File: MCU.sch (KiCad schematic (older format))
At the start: 32 parts, among them J1 RX, J15 RESET, J16 ISP, J17 WS2812, J18 SJ-43514-SMT, J2 TX, J7 TYPE-C-31-M-12, SW1 EC11E, SW3 Reset, U1 ATmega32U4-AU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

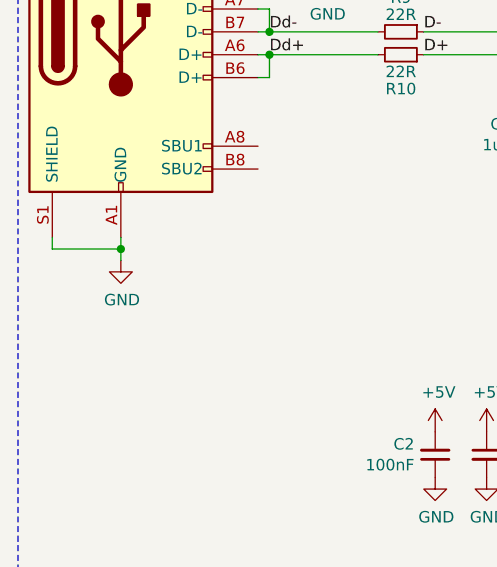
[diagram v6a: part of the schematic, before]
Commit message: Connected USB shield via RC filter, updated renders
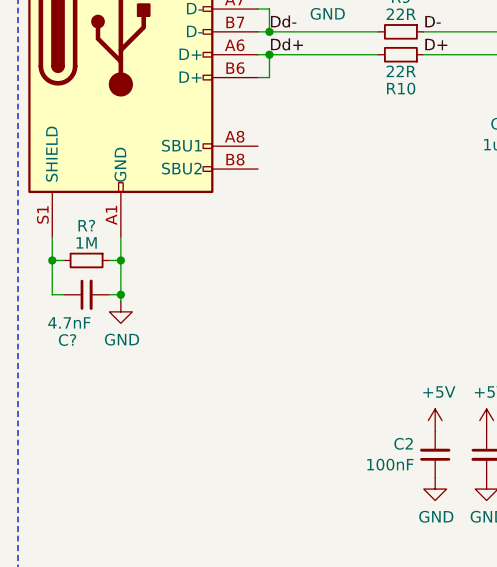
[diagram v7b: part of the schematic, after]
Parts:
- added C?: 4.7nF, Capacitor_SMD:C_0603_1608Metric_Pad1.05x0.95mm_HandSolder, symbol Device:C_Small
- added R?: 1M, Resistor_SMD:R_0603_1608Metric_Pad1.05x0.95mm_HandSolder, symbol Device:R_Small
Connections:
- net GND: now also C?.2, R?.1; no longer J7.S1 (SHIELD)
- new net: C?.1, J7.S1 (SHIELD), R?.2
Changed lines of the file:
@@
 L power:GND #PWR0105
 U 1 1 5DCBF496
-P 1700 3150
+P 1700 3325
 AR Path="/5DCB7F8C/5DCBF496" Ref="#PWR0105"  Part="1"
 AR Path="/5E0F7128/5DCBF496" Ref="#PWR0131"  Part="1"
-F 0 "#PWR0105" H 1700 2900 50  0001 C CNN
-F 1 "GND" H 1705 2977 50  0000 C CNN
-F 2 "" H 1700 3150 50  0001 C CNN
-F 3 "" H 1700 3150 50  0001 C CNN
-	1    1700 3150
-	1    0    0    -1
-$EndComp
-Wire Wire Line
-	1700 3050 1700 3100
-Wire Wire Line
-	1700 3100 1400 3100
-Wire Wire Line
-	1400 3100 1400 3050
-Connection ~ 1700 3100
-Wire Wire Line
-	1700 3100 1700 3150
+F 0 "#PWR0105" H 1700 3075 50  0001 C CNN
+F 1 "GND" H 1705 3152 50  0000 C CNN
+F 2 "" H 1700 3325 50  0001 C CNN
+F 3 "" H 1700 3325 50  0001 C CNN
+	1    1700 3325
+	1    0    0    -1
+$EndComp
 $Comp
 L Device:R_Small R9
@@
 Text Notes 2400 1525 0    50   ~ 0
 1A hold
+$Comp
+L Device:C_Small C?
+U 1 1 5DC857C3
+P 1550 3300
+AR Path="/5DCB7F8C/5DC857C3" Ref="C?"  Part="1"
+AR Path="/5E0F7128/5DC857C3" Ref="C?"  Part="1"
+F 0 "C?" V 1350 3425 50  0000 R CNN
+F 1 "4.7nF" V 1425 3375 50  0000 C CNN
+F 2 "Capacitor_SMD:C_0603_1608Metric_Pad1.05x0.95mm_HandSolder" H 1550 3300 50  0001 C CNN
+F 3 "~" H 1550 3300 50  0001 C CNN
+	1    1550 3300
+	0    -1   -1   0
+$EndComp
+Wire Wire Line
+	1700 3050 1700 3150
+$Comp
+L Device:R_Small R?
+U 1 1 5DCA8592
+P 1550 3150
+AR Path="/5DCB7F8C/5DCA8592" Ref="R?"  Part="1"
+AR Path="/5E0F7128/5DCA8592" Ref="R?"  Part="1"
+F 0 "R?" V 1400 3150 50  0000 C CNN
+F 1 "1M" V 1475 3150 50  0000 C CNN
+F 2 "Resistor_SMD:R_0603_1608Metric_Pad1.05x0.95mm_HandSolder" H 1550 3150 50  0001 C CNN
+F 3 "~" H 1550 3150 50  0001 C CNN
+	1    1550 3150
+	0    1    1    0
+$EndComp
+Wire Wire Line
+	1400 3150 1450 3150
+Wire Wire Line
+	1400 3050 1400 3150
+Wire Wire Line
+	1650 3150 1700 3150
+Wire Wire Line
+	1400 3150 1400 3300
+Wire Wire Line
+	1400 3300 1450 3300
+Connection ~ 1400 3150
+Wire Wire Line
+	1650 3300 1700 3300
+Wire Wire Line
+	1700 3300 1700 3150
+Connection ~ 1700 3150
+Wire Wire Line
+	1700 3325 1700 3300
+Connection ~ 1700 3300
 $EndSCHEMATC

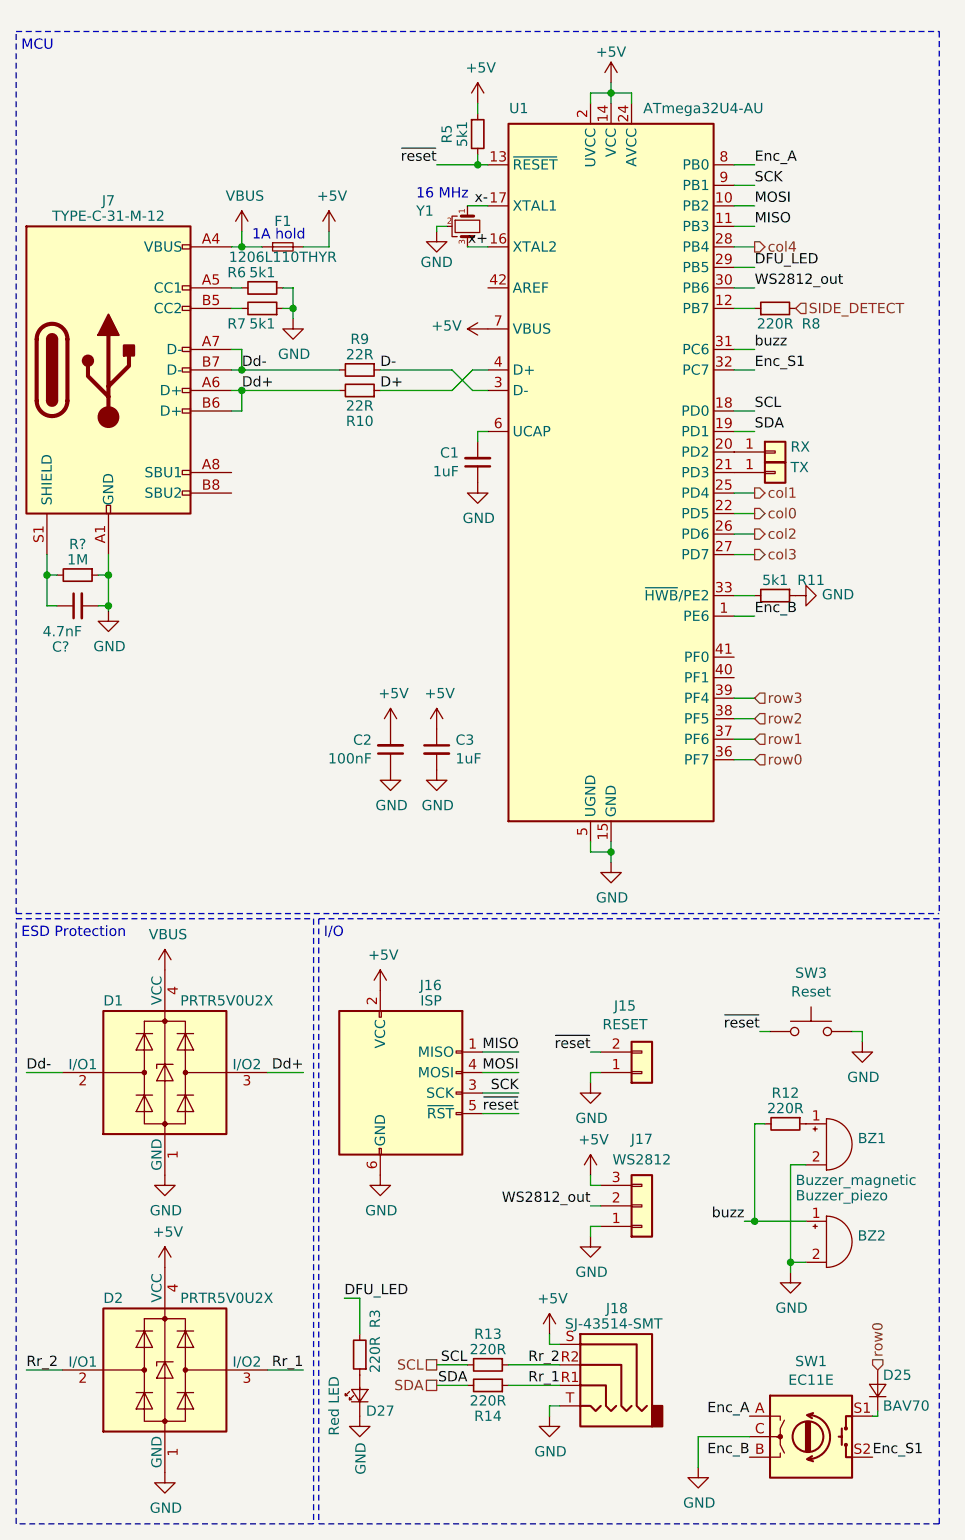
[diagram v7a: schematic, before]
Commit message: Swapped SDA and SCL pins on TRRS jack
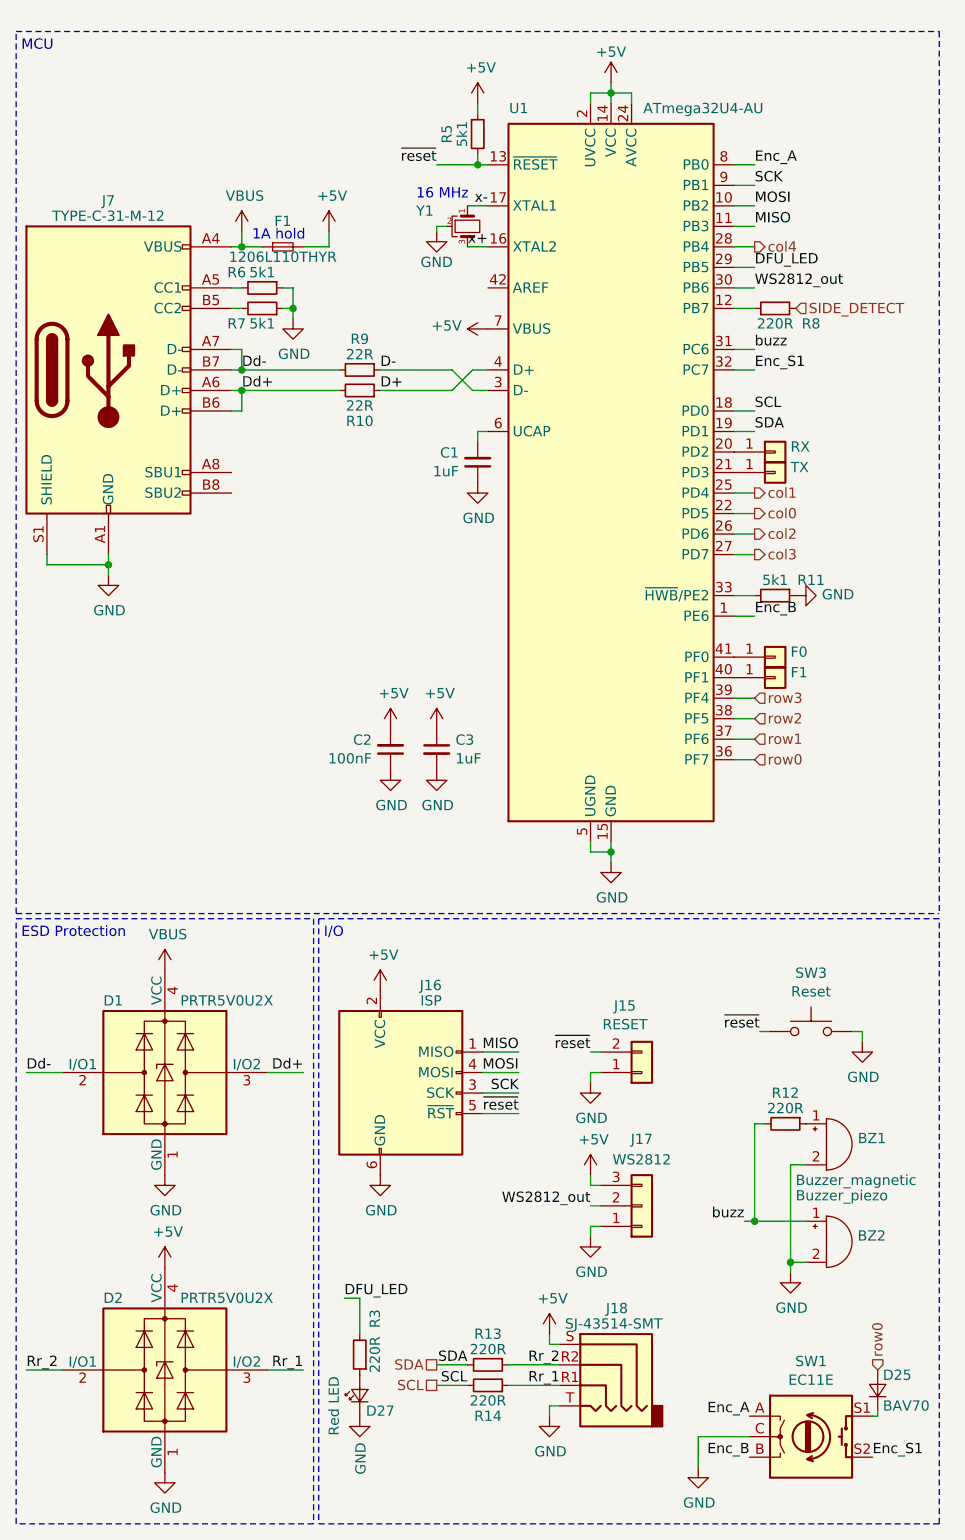
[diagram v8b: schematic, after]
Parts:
- removed C?: 4.7nF, Capacitor_SMD:C_0603_1608Metric_Pad1.05x0.95mm_HandSolder, symbol Device:C_Small
- removed R?: 1M, Resistor_SMD:R_0603_1608Metric_Pad1.05x0.95mm_HandSolder, symbol Device:R_Small
- added J?: F0, TestPoint:TestPoint_Pad_D1.0mm, symbol Connector_Generic:Conn_01x01
- added J?: F1, TestPoint:TestPoint_Pad_D1.0mm, symbol Connector_Generic:Conn_01x01
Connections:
- net GND: now also J7.S1 (SHIELD)
- net SCL: now also R14.2; no longer R13.2
- net SDA: now also R13.2; no longer R14.2
- net at U1.40 (PF1): now also J?.1 (Pin_1)
- net at U1.41 (PF0): now also J?.1 (Pin_1)
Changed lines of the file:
@@
 $EndDescr
-$Comp
-L Connector:USB_C_Receptacle_USB2.0 J7
-U 1 1 5DCB829A
-P 1700 2150
-AR Path="/5DCB7F8C/5DCB829A" Ref="J7"  Part="1"
-AR Path="/5E0F7128/5DCB829A" Ref="J25"  Part="1"
-F 0 "J7" H 1700 2975 50  0000 C CNN
-F 1 "TYPE-C-31-M-12" H 1700 2900 50  0000 C CNN
-F 2 "Connector_USB:USB_C_Receptacle_HRO_TYPE-C-31-M-12" H 1850 2150 50  0001 C CNN
-F 3 "https://www.usb.org/sites/default/files/documents/usb_type-c.zip" H 1850 2150 50  0001 C CNN
-	1    1700 2150
-	1    0    0    -1
-$EndComp
 $Comp
 L Device:R_Small R6
@@
 L power:GND #PWR0105
 U 1 1 5DCBF496
-P 1700 3325
+P 1700 3150
 AR Path="/5DCB7F8C/5DCBF496" Ref="#PWR0105"  Part="1"
 AR Path="/5E0F7128/5DCBF496" Ref="#PWR0131"  Part="1"
-F 0 "#PWR0105" H 1700 3075 50  0001 C CNN
-F 1 "GND" H 1705 3152 50  0000 C CNN
-F 2 "" H 1700 3325 50  0001 C CNN
-F 3 "" H 1700 3325 50  0001 C CNN
-	1    1700 3325
+F 0 "#PWR0105" H 1700 2900 50  0001 C CNN
+F 1 "GND" H 1705 2977 50  0000 C CNN
+F 2 "" H 1700 3150 50  0001 C CNN
+F 3 "" H 1700 3150 50  0001 C CNN
+	1    1700 3150
 	1    0    0    -1
 $EndComp
@@
 Text Label 4050 6225 2    50   ~ 0
 WS2812_out
+Text Label 3450 7000 2    50   ~ 0
+SDA
 Text Label 3450 7100 2    50   ~ 0
-SDA
-Text Label 3450 7000 2    50   ~ 0
 SCL
 Text Label 3900 7000 2    50   ~ 0
@@
 Wire Wire Line
 	3300 7100 3450 7100
+Text HLabel 3300 7100 0    50   UnSpc ~ 0
+SCL
 Text HLabel 3300 7000 0    50   UnSpc ~ 0
-SCL
-Text HLabel 3300 7100 0    50   UnSpc ~ 0
 SDA
 $Comp
@@
 Text Notes 2400 1525 0    50   ~ 0
 1A hold
-$Comp
-L Device:C_Small C?
-U 1 1 5DC857C3
-P 1550 3300
-AR Path="/5DCB7F8C/5DC857C3" Ref="C?"  Part="1"
-AR Path="/5E0F7128/5DC857C3" Ref="C?"  Part="1"
-F 0 "C?" V 1350 3425 50  0000 R CNN
-F 1 "4.7nF" V 1425 3375 50  0000 C CNN
-F 2 "Capacitor_SMD:C_0603_1608Metric_Pad1.05x0.95mm_HandSolder" H 1550 3300 50  0001 C CNN
-F 3 "~" H 1550 3300 50  0001 C CNN
-	1    1550 3300
-	0    -1   -1   0
-$EndComp
-Wire Wire Line
-	1700 3050 1700 3150
-$Comp
-L Device:R_Small R?
-U 1 1 5DCA8592
-P 1550 3150
-AR Path="/5DCB7F8C/5DCA8592" Ref="R?"  Part="1"
-AR Path="/5E0F7128/5DCA8592" Ref="R?"  Part="1"
-F 0 "R?" V 1400 3150 50  0000 C CNN
-F 1 "1M" V 1475 3150 50  0000 C CNN
-F 2 "Resistor_SMD:R_0603_1608Metric_Pad1.05x0.95mm_HandSolder" H 1550 3150 50  0001 C CNN
-F 3 "~" H 1550 3150 50  0001 C CNN
-	1    1550 3150
-	0    1    1    0
-$EndComp
-Wire Wire Line
-	1400 3150 1450 3150
-Wire Wire Line
-	1400 3050 1400 3150
-Wire Wire Line
-	1650 3150 1700 3150
-Wire Wire Line
-	1400 3150 1400 3300
-Wire Wire Line
-	1400 3300 1450 3300
-Connection ~ 1400 3150
-Wire Wire Line
-	1650 3300 1700 3300
-Wire Wire Line
-	1700 3300 1700 3150
-Connection ~ 1700 3150
-Wire Wire Line
-	1700 3325 1700 3300
-Connection ~ 1700 3300
+Wire Wire Line
+	1700 3050 1700 3100
+$Comp
+L Connector:USB_C_Receptacle_USB2.0 J7
+U 1 1 5DCB829A
+P 1700 2150
+AR Path="/5DCB7F8C/5DCB829A" Ref="J7"  Part="1"
+AR Path="/5E0F7128/5DCB829A" Ref="J25"  Part="1"
+F 0 "J7" H 1700 2975 50  0000 C CNN
+F 1 "TYPE-C-31-M-12" H 1700 2900 50  0000 C CNN
+F 2 "Connector_USB:USB_C_Receptacle_HRO_TYPE-C-31-M-12" H 1850 2150 50  0001 C CNN
+F 3 "https://www.usb.org/sites/default/files/documents/usb_type-c.zip" H 1850 2150 50  0001 C CNN
+	1    1700 2150
+	1    0    0    -1
+$EndComp
+Wire Wire Line
+	1400 3050 1400 3100
+Wire Wire Line
+	1400 3100 1700 3100
+Connection ~ 1700 3100
+Wire Wire Line
+	1700 3100 1700 3150
+$Comp
+L Connector_Generic:Conn_01x01 J?
+U 1 1 5DCC64E4
+P 4950 3550
+AR Path="/5DCB7F8C/5DCC64E4" Ref="J?"  Part="1"
+AR Path="/5E0F7128/5DCC64E4" Ref="J?"  Part="1"
+F 0 "J?" H 4900 3650 50  0001 L CNN
+F 1 "F0" H 5025 3575 50  0000 L CNN
+F 2 "TestPoint:TestPoint_Pad_D1.0mm" H 4950 3550 50  0001 C CNN
+F 3 "~" H 4950 3550 50  0001 C CNN
+	1    4950 3550
+	1    0    0    -1
+$EndComp
+$Comp
+L Connector_Generic:Conn_01x01 J?
+U 1 1 5DCC6DF3
+P 4950 3650
+AR Path="/5DCB7F8C/5DCC6DF3" Ref="J?"  Part="1"
+AR Path="/5E0F7128/5DCC6DF3" Ref="J?"  Part="1"
+F 0 "J?" H 4900 3750 50  0001 L CNN
+F 1 "F1" H 5025 3675 50  0000 L CNN
+F 2 "TestPoint:TestPoint_Pad_D1.0mm" H 4950 3650 50  0001 C CNN
+F 3 "~" H 4950 3650 50  0001 C CNN
+	1    4950 3650
+	1    0    0    -1
+$EndComp
 $EndSCHEMATC
